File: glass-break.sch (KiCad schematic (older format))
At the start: 4 parts

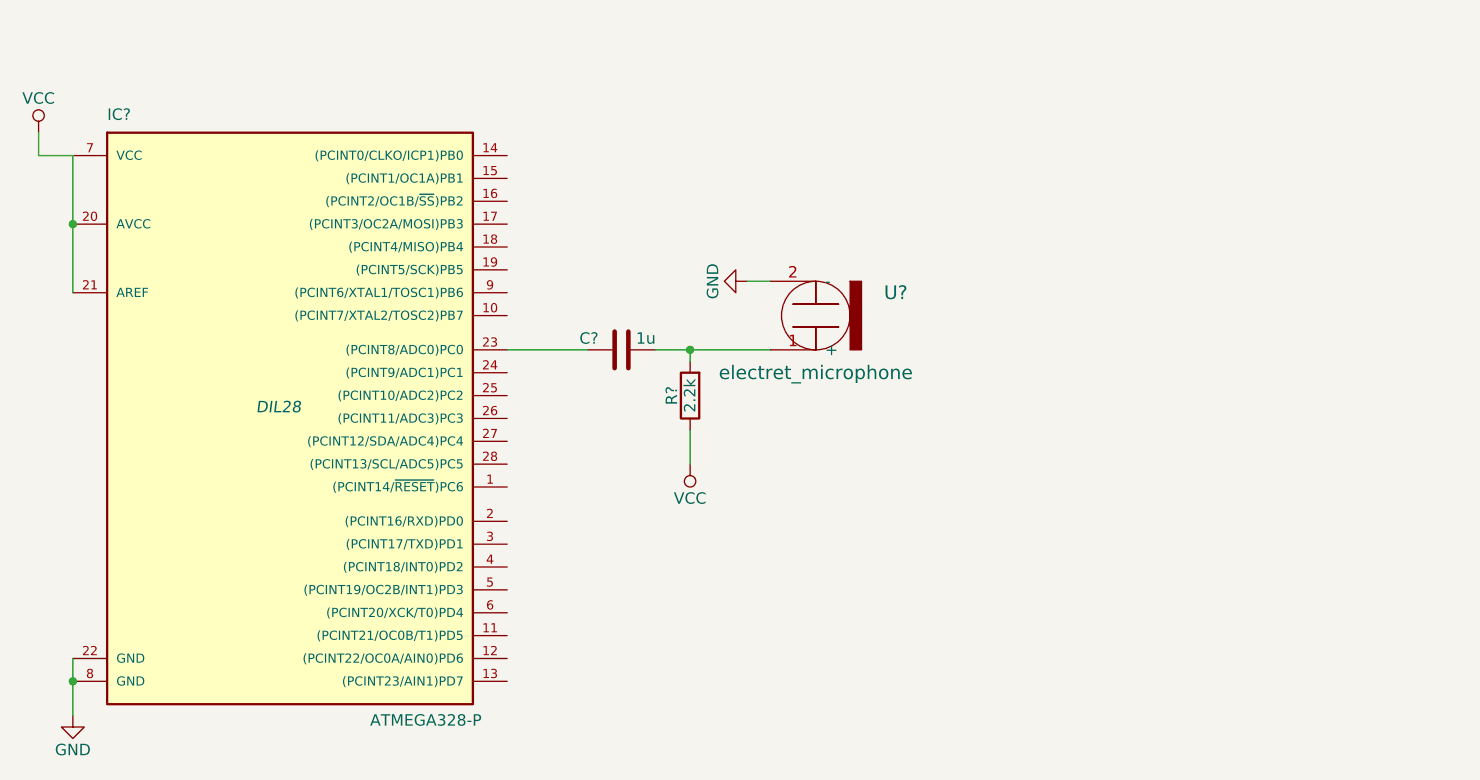
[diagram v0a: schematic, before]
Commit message: added schematic components
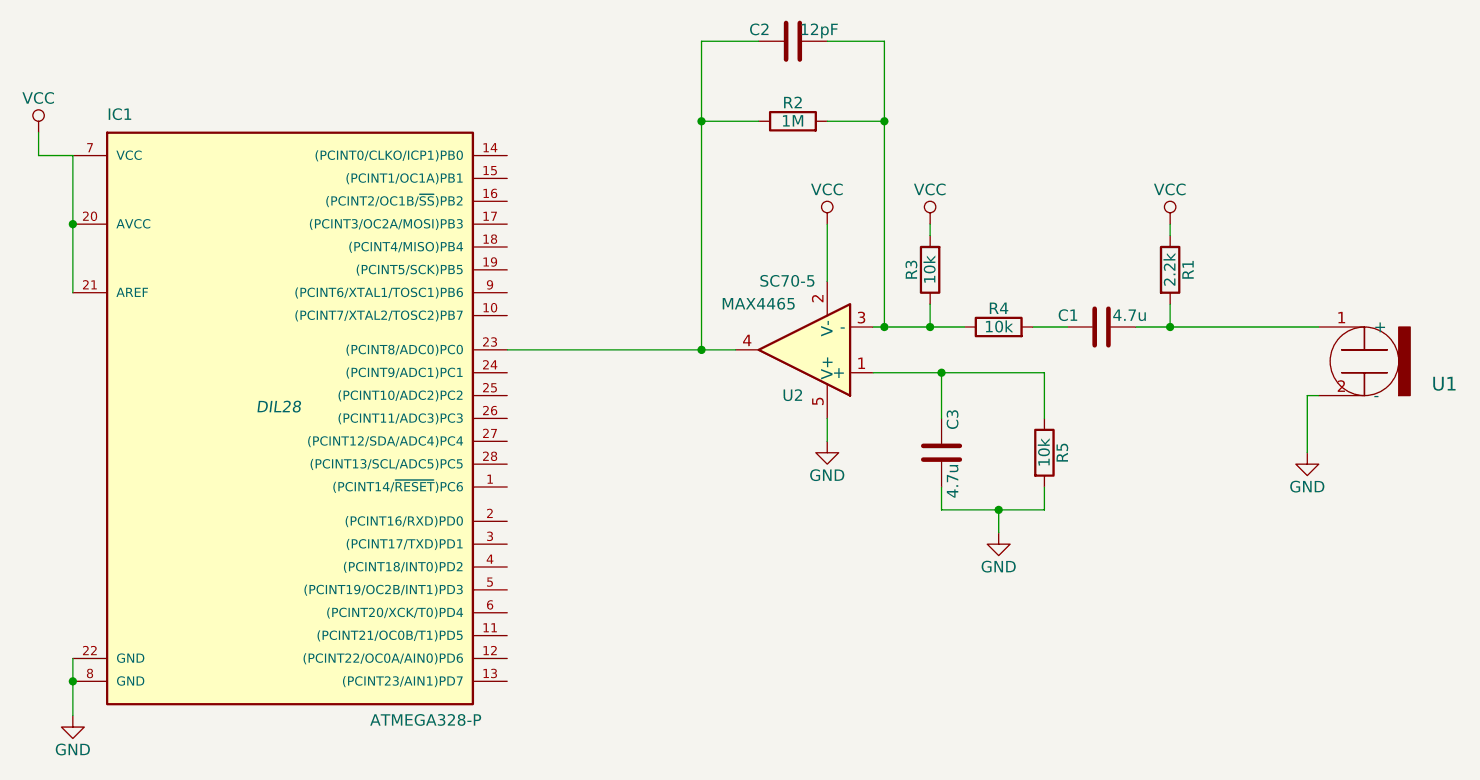
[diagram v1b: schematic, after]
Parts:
- added C2: 12pF, symbol C
- added C3: 4.7u, symbol C
- added R2: 1M, symbol R
- added R3, R4, R5: 10k, symbol R
- added U2: MAX4465, SC70-5, symbol OPA376AIDCK
- C1: renamed from C?; value 1u -> 4.7u
- gave numbers to parts that had none: 3
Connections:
- net GND: now also C3.2, R5.2, U2.5 (V+)
- net VCC: now also R3.2, U2.2 (V-)
- net at IC1.23 ((PCINT8/ADC0)PC0): now also C2.1, R2.1, U2.4; no longer C1.1
- new net: C1.1, R4.2
- new net: C2.2, R2.2, R3.1, R4.1, U2.3 (-)
- new net: C3.1, R5.1, U2.1 (+)
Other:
- moved on the sheet: C1, R1, U1
